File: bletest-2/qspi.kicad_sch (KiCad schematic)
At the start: 4 parts, among them J2 Conn_01x02, U4 W25Q128JVP

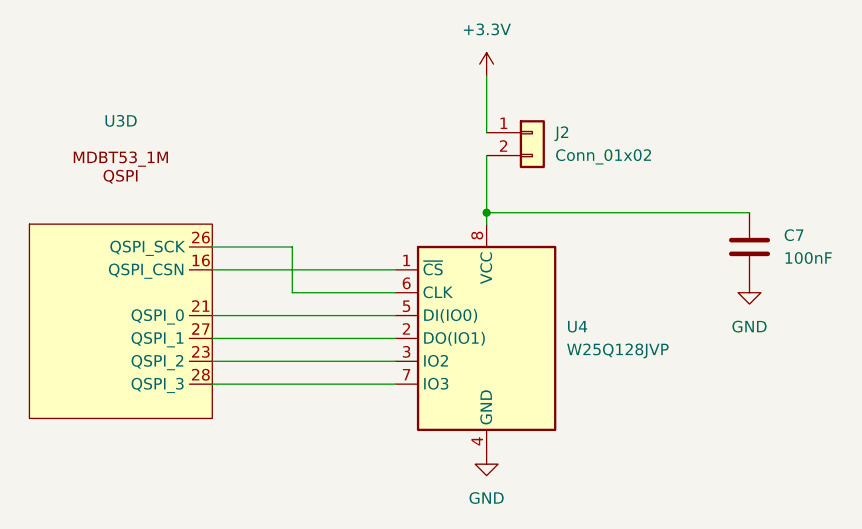
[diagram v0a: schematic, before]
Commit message: Full routing done
There are still a bunch of ERC violations.
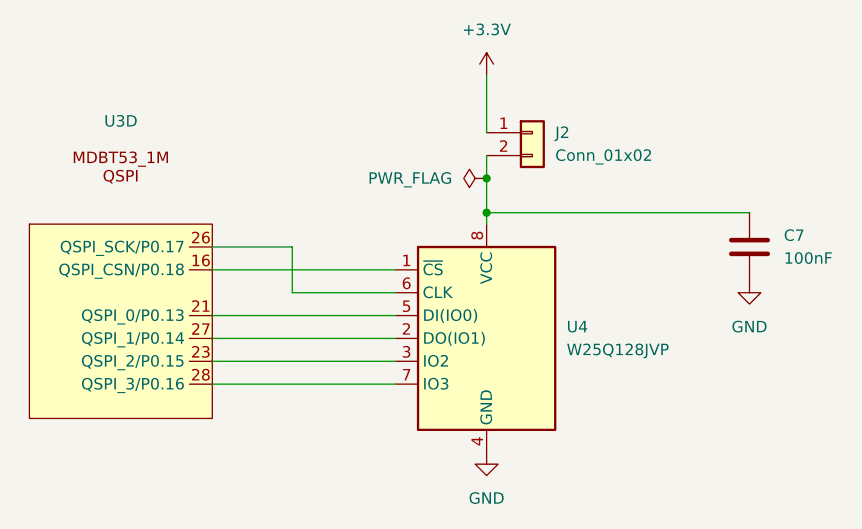
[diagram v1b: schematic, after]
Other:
- moved on the sheet: U3D
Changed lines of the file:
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@@
 		(color 0 0 0 0)
 	)
+	(junction
+		(at 114.3 64.77)
+		(diameter 0)
+		(color 0 0 0 0)
+	)
 	(wire
 		(pts
@@
 	(wire
 		(pts
+			(xy 114.3 64.77) (xy 114.3 68.58)
+		)
+		(stroke
+			(width 0)
+			(type default)
+		)
+	)
+	(wire
+		(pts
 			(xy 92.71 77.47) (xy 104.14 77.47)
 		)
@@
 	(wire
 		(pts
-			(xy 114.3 62.23) (xy 114.3 68.58)
+			(xy 114.3 62.23) (xy 114.3 64.77)
 		)
 		(stroke
@@
 		(pin "16"
 		)
-		(pin "21"
-		)
-		(pin "23"
-		)
-		(pin "26"
-		)
 		(pin "27"
 		)
@@
 		(pin "13"
 		)
+		(pin "15"
+		)
+		(pin "18"
+		)
+		(pin "29"
+		)
+		(pin "30"
+		)
+		(pin "32"
+		)
+		(pin "44"
+		)
+		(pin "46"
+		)
+		(pin "48"
+		)
+		(pin "55"
+		)
+		(pin "59"
+		)
+		(pin "63"
+		)
+		(pin "64"
+		)
+		(pin "24"
+		)
+		(pin "54"
+		)
+		(pin "61"
+		)
+		(pin "41"
+		)
+		(pin "58"
+		)
+		(pin "50"
+		)
+		(pin "40"
+		)
+		(pin "42"
+		)
+		(pin "52"
+		)
+		(pin "38"
+		)
 		(pin "14"
-		)
-		(pin "15"
-		)
-		(pin "16"
-		)
-		(pin "17"
-		)
-		(pin "18"
-		)
-		(pin "27"
-		)
-		(pin "28"
-		)
-		(pin "29"
-		)
-		(pin "30"
-		)
-		(pin "32"
-		)
-		(pin "39"
-		)
-		(pin "5"
-		)
-		(pin "60"
-		)
-		(pin "7"
-		)
-		(pin "9"
-		)
-		(pin "44"
-		)
-		(pin "46"
-		)
-		(pin "48"
-		)
-		(pin "55"
-		)
-		(pin "59"
-		)
-		(pin "63"
-		)
-		(pin "64"
-		)
-		(pin "20"
-		)
-		(pin "35"
-		)
-		(pin "37"
-		)
-		(pin "24"
-		)
-		(pin "54"
-		)
-		(pin "61"
-		)
-		(pin "41"
-		)
-		(pin "58"
-		)
-		(pin "50"
-		)
-		(pin "40"
-		)
-		(pin "42"
-		)
-		(pin "52"
-		)
-		(pin "38"
 		)
 		(instances
@@
 				)
 			)
+		)
+	)
+	(symbol
+		(lib_id "power:PWR_FLAG")
+		(at 114.3 64.77 90)
+		(unit 1)
+		(exclude_from_sim no)
+		(in_bom yes)
+		(on_board yes)
+		(dnp no)
+		(fields_autoplaced yes)
+		(property "Reference" "#FLG08"
+			(at 112.395 64.77 0)
+			(effects
+				(font
+					(size 1.27 1.27)
+				)
+				(hide yes)
+			)
+		)
+		(property "Value" "PWR_FLAG"
+			(at 110.49 64.7699 90)
+			(effects
+				(font
+					(size 1.27 1.27)
+				)
+				(justify left)
+			)
+		)
+		(property "Footprint" ""
+			(at 114.3 64.77 0)
+			(effects
+				(font
+					(size 1.27 1.27)
+				)
+				(hide yes)
+			)
+		)
+		(property "Datasheet" "~"
+			(at 114.3 64.77 0)
+			(effects
+				(font
+					(size 1.27 1.27)
+				)
+				(hide yes)
+			)
+		)
+		(property "Description" "Special symbol for telling ERC where power comes from"
+			(at 114.3 64.77 0)
+			(effects
+				(font
+					(size 1.27 1.27)
+				)
+				(hide yes)
+			)
+		)
+		(pin "1"
+		)
+		(instances
+			(project "bletest-2"
+				(path "/8765e634-cc5d-4e93-a9fe-a7a0a02791b6/1b765584-d95c-49e7-9dfc-58741c7180f6"
+					(reference "#FLG08")
+					(unit 1)
+				)
+			)

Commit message: Rev A of bletest
Finish cleanup, and remove last remaining violations.

There are a handful of silkscreen overlaps with explicit exclusions.
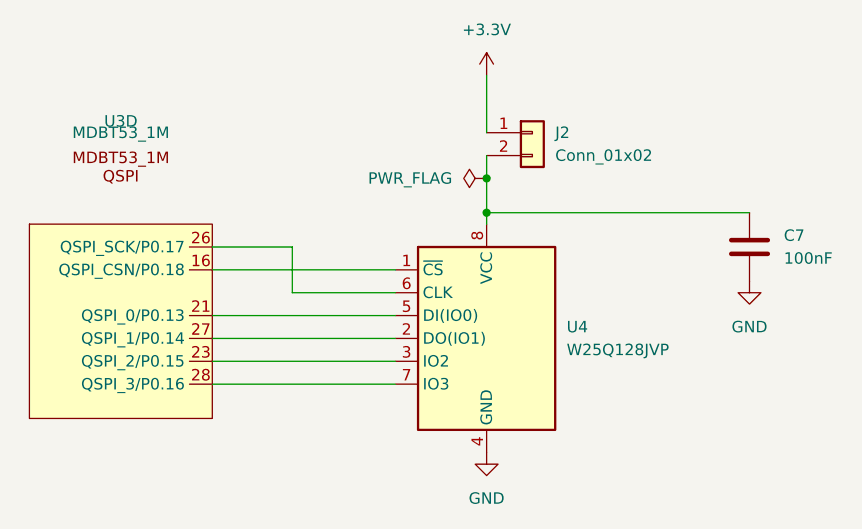
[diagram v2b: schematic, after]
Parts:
- U3: value ~ -> MDBT53_1M
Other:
- company: (none) -> David Brown
- title: (none) -> BLETEXT-2
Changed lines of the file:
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@@
 	(generator "eeschema")
 	(generator_version "8.0")
-	(paper "A4")
+	(paper "A")
+	(title_block
+		(title "BLETEXT-2")
+		(date "2024-12-07")
+		(rev "REVA")
+		(company "David Brown")
+	)
 	(junction
 		(at 114.3 68.58)
@@
 			)
 		)
-		(property "Value" "~"
+		(property "Value" "MDBT53_1M"
 			(at 73.66 59.69 0)
 			(effects
@@
 			)
 		)
-		(property "Datasheet" ""
+		(property "Datasheet" "https://www.amazon.com/dp/B0B4BC8Z1V"
 			(at 73.66 82.55 0)
 			(effects
@@
 			)
 		)
-		(property "Datasheet" "~"
+		(property "Datasheet" "https://www.digikey.com/en/products/detail/yageo/CC0603KRX7R7BB104/302822"
 			(at 143.51 72.39 0)
 			(effects
@@
 			)
 		)
-		(property "Datasheet" "https://www.winbond.com/resource-files/w25q128jv_dtr%20revc%2003272018%20plus.pdf"
+		(property "Datasheet" "https://www.digikey.com/en/products/detail/winbond-electronics/W25Q128JVPIQ/6819668"
 			(at 114.3 57.15 0)
 			(effects
